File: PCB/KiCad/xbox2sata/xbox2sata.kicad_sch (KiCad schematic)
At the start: 45 parts, among them J1 61203921621, J2 67800-8025, J3 90151-2140, U1 1V2 voltage regulator, U5 88SA8052, Y1 25MHz

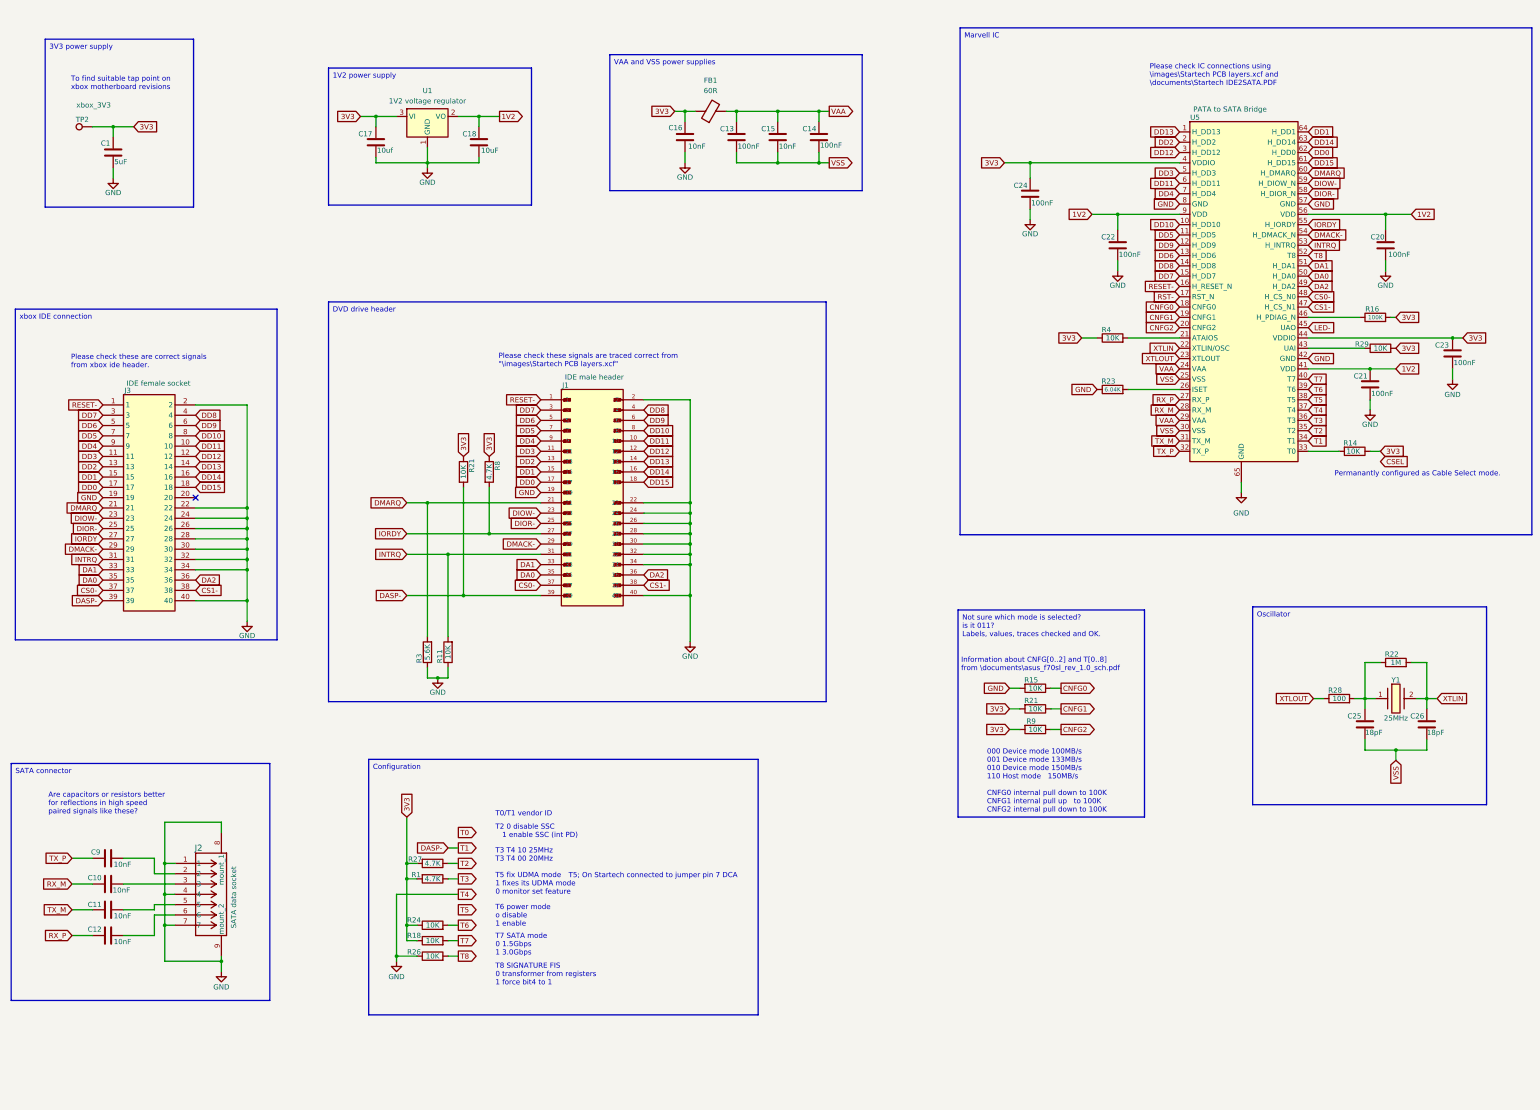
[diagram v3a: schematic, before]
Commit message: bill of matierals
spreadsheet for bill of materials,
IDE female socket changed to cheaper option,
SATA socket changed to right angle, recommend by doofus.
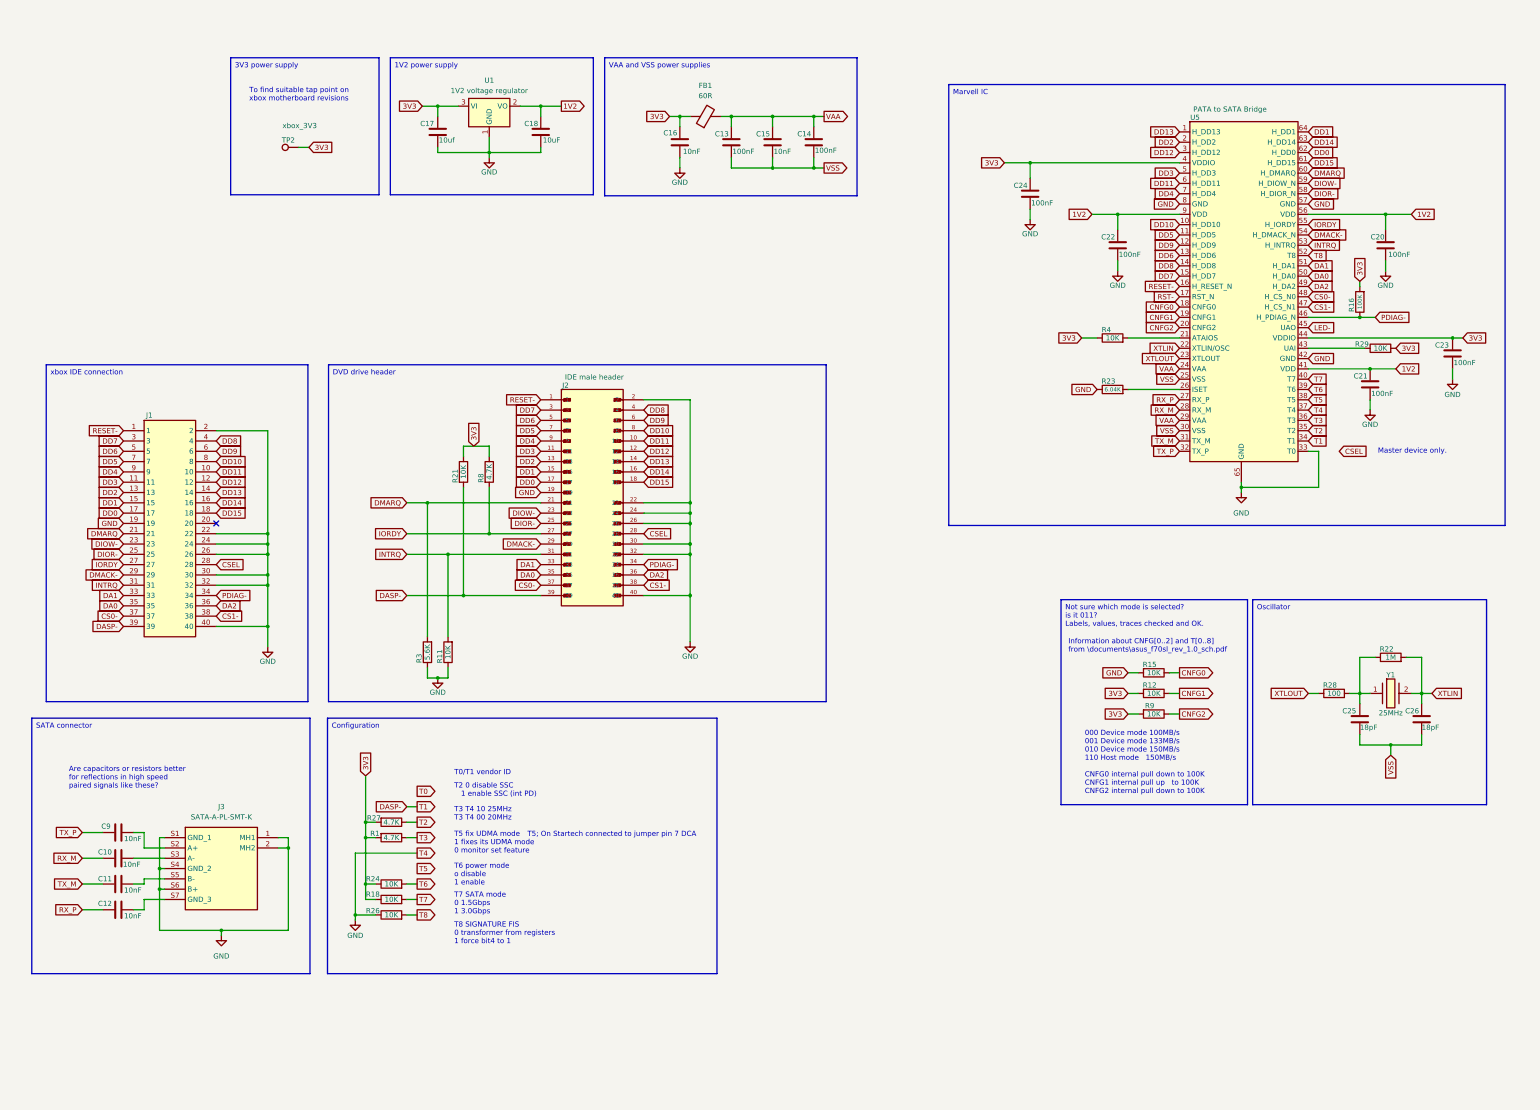
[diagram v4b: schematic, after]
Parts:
- removed C1: 5uF, Capacitor_SMD:C_0402_1005Metric_Pad0.74x0.62mm_HandSolder, symbol Device:C
- removed J2: 67800-8025, xbox2sata:CONN_67800-8025_MOL, symbol xbox2sata:67800-8025
- removed J3: 90151-2140, xbox2sata:RHDR40W70P254_2X20_5065X498X870P, symbol xbox2sata:90151-2140
- removed R14: 10K, symbol Device:R
- added J1: 929975-01-20-RK, xbox2sata:RHDR40W76P254_2X20_5080X508X826P, symbol xbox2sata:929975-01-20-RK
- added J3: SATA-A-PL-SMT-K, SATAAPLSMTK, symbol xbox2sata:SATA-A-PL-SMT-K
- FB1: footprint (none) -> Resistor_SMD:R_0402_1005Metric_Pad0.72x0.64mm_HandSolder
- U1: footprint Package_TO_SOT_SMD:SOT-223-3_TabPin2 -> Package_TO_SOT_SMD:SOT-89-3_Handsoldering
- Y1: Manufacturer_Part_Number ABLS-25.000MHZ-B4-F-T -> ABLS-25.000MHZ-16-A-4-H-F-T; Mouser Part Number 815-ABLS-25.0M-F-T -> 815-ABLS25MHZ16A4HFT; Mouser Price/Stock https://www.mouser.co.uk/ProductDetail/ABRACON/ABLS-25.000MHZ-B4-F-T?qs=yTU0IcKoRlHGW93axwFkQw%3D%3D -> https://www.mouser.co.uk/ProductDetail/ABRACON/ABLS-25.000MHZ-16-A-4-H-F-T?qs=vLWxofP3U2wYSEjvdJ0sYQ%3D%3D
- renumbered J1 to J2, R21 to R12
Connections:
- net CS0-: now also J1.37
- net CS1-: now also J1.38
- net CSEL: now also J2.28, J1.28
- net DA0: now also J1.35
- net DA1: now also J1.33
- net DA2: now also J1.36
- net DASP-: now also J1.39
- net DD0: now also J1.17
- net DD1: now also J1.15
- net DD10: now also J1.8
- net DD11: now also J1.10
- net DD12: now also J1.12
- net DD13: now also J1.14
- net DD14: now also J1.16
- net DD15: now also J1.18
- net DD2: now also J1.13
- net DD3: now also J1.11
- net DD4: now also J1.9
- net DD5: now also J1.7
- net DD6: now also J1.5
- net DD7: now also J1.3
- net DD8: now also J1.4
- net DD9: now also J1.6
- net DIOR-: now also J1.25
- net DIOW-: now also J1.23
- net DMACK-: now also J1.29
- net DMARQ: now also J1.21
- net GND: now also U5.33 (T0), J1.19, J1.2, J1.22, J1.24, J1.26, J1.30, J1.32, J1.40, J3.1 (MH1), J3.2 (MH2), J3.S1 (GND_1), J3.S4 (GND_2), J3.S6 (B+); no longer J2.28, J2.34
- net INTRQ: now also J1.31
- net IORDY: now also J1.27
- net RESET-: now also J1.1
- net PDIAG-: now reaches R16.1, U5.46 (H_PDIAG_N)
- net PDIAG-: now also J2.34, J1.34
- net at C9.2: now also J3.S2 (A+)
- net at C10.2: now also J3.S3 (A-)
- net at C11.2: now also J3.S5 (B-)
- net at C12.2: now also J3.S7 (GND_3)
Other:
- note added: "Master device only."
- note removed: "Permanantly configured as Cable Select mode."
- note removed: "Please check IC connections using \images\Startech PCB layers.xcf and \documents\Startech IDE2SATA.PDF"
- note removed: "Please check these are correct signals from xbox ide header."
- note removed: "Please check these signals are traced correct from "\images\Startech PCB layers.xcf""
- moved on the sheet: C10, C11, C12, C13, C14, C15, C16, C17, C18, C25, C26, C9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

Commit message: reset and csel correct circuit from startech
10K resistor (R14) pull-up to 3V3 added to CSEL IDE pin 28
4.7K resistor (R19) pull-down to ground on T0 U5 pin 33 to device as IDE master
positive power supply icons changed from Global labels to power symbols
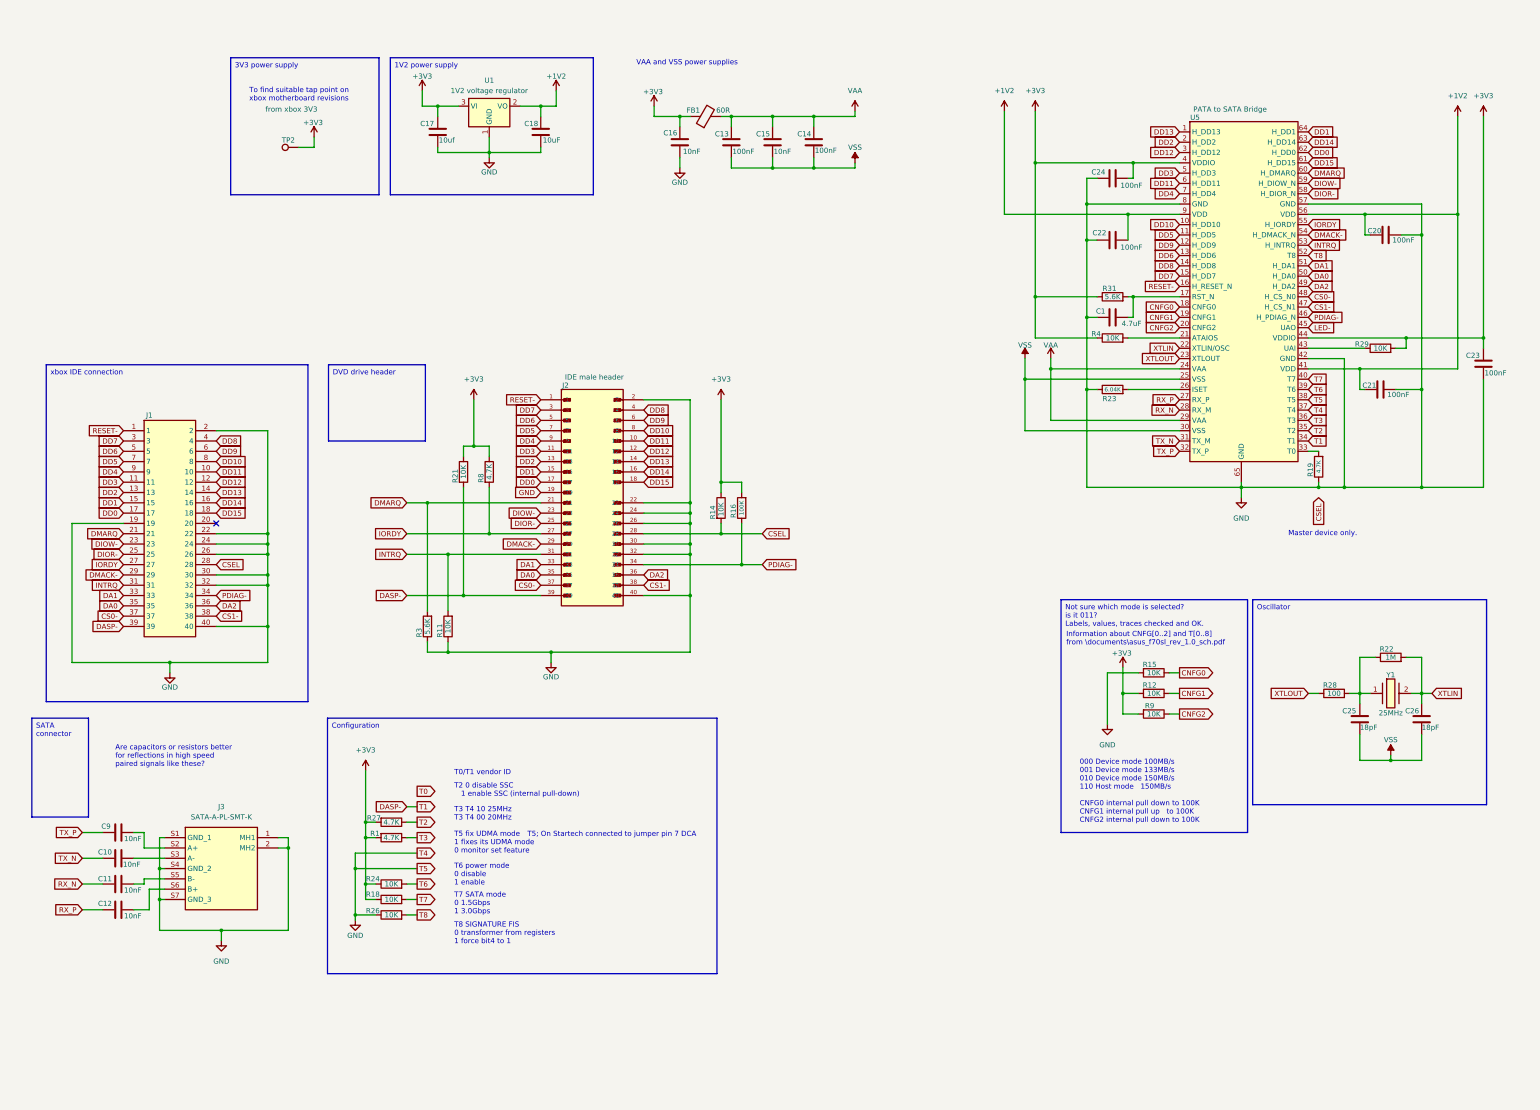
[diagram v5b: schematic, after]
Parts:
- added C1: 4.7uF, Capacitor_SMD:C_0402_1005Metric_Pad0.74x0.62mm_HandSolder, symbol Device:C
- added R14: 10K, Resistor_SMD:R_0402_1005Metric_Pad0.72x0.64mm_HandSolder, symbol Device:R
- added R19: 4.7K, Resistor_SMD:R_0402_1005Metric_Pad0.72x0.64mm_HandSolder, symbol Device:R
- added R31: 5.6K, Resistor_SMD:R_0402_1005Metric_Pad0.72x0.64mm_HandSolder, symbol Device:R
- TP2: value xbox_3V3 -> from xbox 3V3
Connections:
- net T5 is gone; now on net GND: U5.38 (T5)
- net CSEL: now also R14.2
- net GND: now also C22.1, C24.1, J3.S7 (GND_3), C1.1, R19.1; no longer C22.2, C24.2, J3.S6 (B+), U5.33 (T0)
- net at C12.2: now also J3.S6 (B+); no longer J3.S7 (GND_3)
- net 1V2 renamed +1V2
- net +1V2: now also C22.2; no longer C22.1
- net 3V3 renamed +3V3
- net +3V3: now also C24.2, R14.1, R31.1; no longer C24.1
- net RST-: no longer names the net of U5.17 (RST_N)
- net RST-: now also C1.2, R31.2
- net RX_M renamed RX_N
- net RX_N: now also C11.1; no longer C10.1
- net TX_M renamed TX_N
- net TX_N: now also C10.1; no longer C11.1
- new net: R19.2, U5.33 (T0)
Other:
- note added: "T2 0 disable SSC 1 enable SSC (internal pull-down)"
- note added: "T6 power mode 0 disable 1 enable"
- note added: "VAA and VSS power supplies"
- note removed: "T2 0 disable SSC 1 enable SSC (int PD)"
- note removed: "T6 power mode o disable 1 enable"
- moved on the sheet: C20, C21, C22, C23, C24, R11, R16, R3
